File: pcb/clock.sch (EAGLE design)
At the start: 20 parts, among them IC1 74AHCT125, U1 ESP-01, U2 LD1117V33

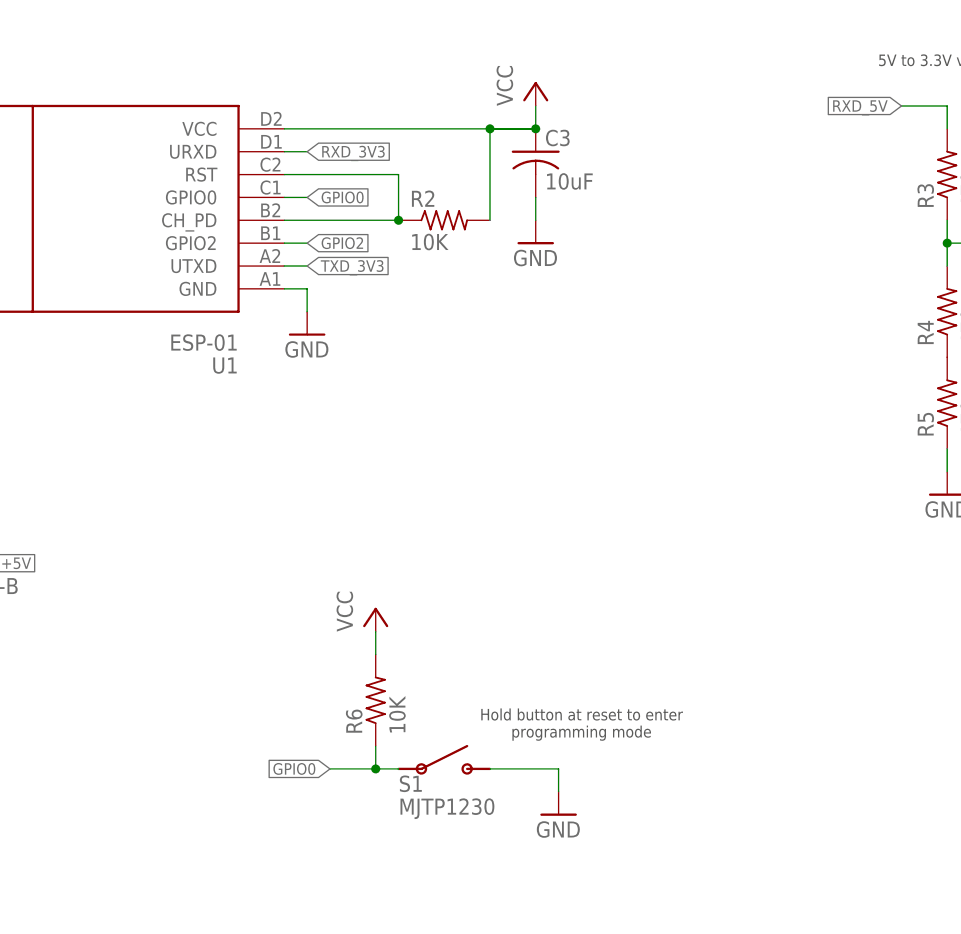
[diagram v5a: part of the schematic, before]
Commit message: Added DTR to RST pin
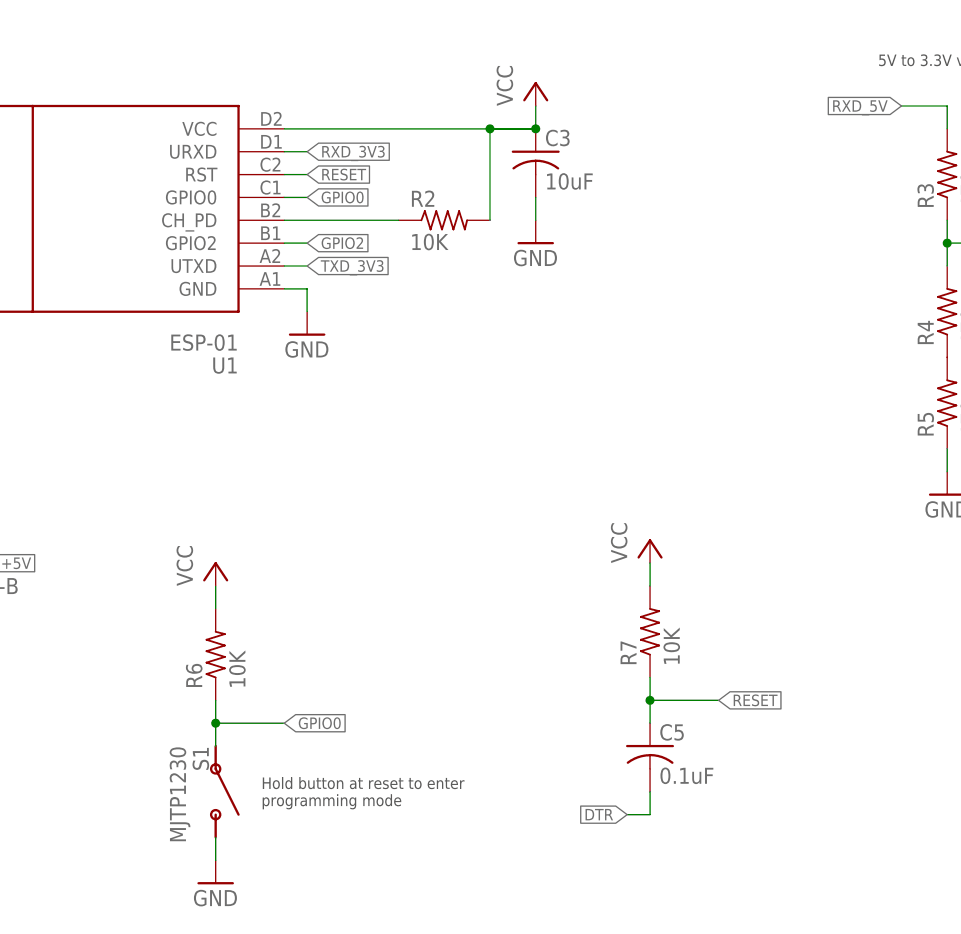
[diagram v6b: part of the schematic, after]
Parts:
- added C5: 0.1uF, rcl:C-US025-025X050
- added R7: 10K, rcl:R-US_0207/10
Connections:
- removed net N$2: R2.1, U1.CH_PD, U1.RST
- new net N$4: R2.1, U1.CH_PD
- new net RESET: C5.1, R7.1, U1.RST
- net DTR: now also C5.2
- net VCC: now also R7.2
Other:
- moved on the sheet: R6, S1
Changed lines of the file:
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@@
 <part name="GND11" library="supply1" deviceset="GND" device=""/>
 <part name="D1" library="diode" deviceset="1N581*" device="" technology="7-B"/>
+<part name="P+4" library="supply1" deviceset="VCC" device=""/>
+<part name="R7" library="rcl" deviceset="R-US_" device="0207/10" value="10K"/>
+<part name="C5" library="rcl" deviceset="C-US" device="025-025X050" value="0.1uF"/>
 </parts>
 <sheets>
 <sheet>
 <plain>
-<text x="114.3" y="40.64" size="1.27" layer="97" align="center">Hold button at reset to enter
+<text x="78.74" y="33.02" size="1.27" layer="97" align="center-left">Hold button at reset to enter
 programming mode</text>
 <text x="157.48" y="114.3" size="1.27" layer="97" align="center">5V to 3.3V voltage divider</text>
@@
 <instance part="IC1" gate="G$1" x="220.98" y="91.44"/>
 <instance part="GND8" gate="1" x="198.12" y="78.74"/>
-<instance part="S1" gate="G$1" x="99.06" y="35.56"/>
+<instance part="S1" gate="G$1" x="73.66" y="33.02" rot="R270"/>
 <instance part="GND9" gate="1" x="35.56" y="25.4"/>
-<instance part="GND10" gate="1" x="111.76" y="30.48"/>
-<instance part="P+3" gate="VCC" x="91.44" y="53.34"/>
-<instance part="R6" gate="G$1" x="91.44" y="43.18" rot="R90"/>
+<instance part="GND10" gate="1" x="73.66" y="22.86"/>
+<instance part="P+3" gate="VCC" x="73.66" y="58.42"/>
+<instance part="R6" gate="G$1" x="73.66" y="48.26" rot="R90"/>
 <instance part="H1" gate="G$1" x="177.8" y="162.56"/>
 <instance part="H2" gate="G$1" x="177.8" y="154.94"/>
 <instance part="GND11" gate="1" x="170.18" y="149.86"/>
 <instance part="D1" gate="G$1" x="43.18" y="58.42"/>
+<instance part="P+4" gate="VCC" x="121.92" y="60.96"/>
+<instance part="R7" gate="G$1" x="121.92" y="50.8" rot="R90"/>
+<instance part="C5" gate="G$1" x="121.92" y="38.1"/>
 </instances>
 <busses>
@@
 <pinref part="P+3" gate="VCC" pin="VCC"/>
 <pinref part="R6" gate="G$1" pin="2"/>
-<wire x1="91.44" y1="50.8" x2="91.44" y2="48.26" width="0.1524" layer="91"/>
+<wire x1="73.66" y1="55.88" x2="73.66" y2="53.34" width="0.1524" layer="91"/>
+</segment>
+<segment>
+<pinref part="P+4" gate="VCC" pin="VCC"/>
+<pinref part="R7" gate="G$1" pin="2"/>
+<wire x1="121.92" y1="58.42" x2="121.92" y2="55.88" width="0.1524" layer="91"/>
 </segment>
 </net>
@@
 <segment>
 <pinref part="S1" gate="G$1" pin="3"/>
-<wire x1="104.14" y1="35.56" x2="111.76" y2="35.56" width="0.1524" layer="91"/>
-<wire x1="111.76" y1="35.56" x2="111.76" y2="33.02" width="0.1524" layer="91"/>
+<wire x1="73.66" y1="27.94" x2="73.66" y2="25.4" width="0.1524" layer="91"/>
 <pinref part="GND10" gate="1" pin="GND"/>
 </segment>
@@
 <wire x1="43.18" y1="43.18" x2="35.56" y2="43.18" width="0.1524" layer="91"/>
 <label x="35.56" y="43.18" size="1.27" layer="95" rot="MR0" xref="yes"/>
+</segment>
+<segment>
+<pinref part="C5" gate="G$1" pin="2"/>
+<wire x1="121.92" y1="33.02" x2="121.92" y2="30.48" width="0.1524" layer="91"/>
+<wire x1="121.92" y1="30.48" x2="119.38" y2="30.48" width="0.1524" layer="91"/>
+<label x="119.38" y="30.48" size="1.27" layer="95" rot="R180" xref="yes"/>
 </segment>
 </net>
@@
 </segment>
 </net>
-<net name="N$2" class="0">
-<segment>
-<pinref part="U1" gate="G$1" pin="CH_PD"/>
-<pinref part="R2" gate="G$1" pin="1"/>
-<wire x1="81.28" y1="96.52" x2="93.98" y2="96.52" width="0.1524" layer="91"/>
-<pinref part="U1" gate="G$1" pin="RST"/>
-<wire x1="81.28" y1="101.6" x2="93.98" y2="101.6" width="0.1524" layer="91"/>
-<wire x1="93.98" y1="101.6" x2="93.98" y2="96.52" width="0.1524" layer="91"/>
-<junction x="93.98" y="96.52"/>
-</segment>
-</net>
 <net name="N$3" class="0">
 <segment>
@@
 <segment>
 <pinref part="S1" gate="G$1" pin="1"/>
-<wire x1="93.98" y1="35.56" x2="91.44" y2="35.56" width="0.1524" layer="91"/>
-<wire x1="91.44" y1="35.56" x2="86.36" y2="35.56" width="0.1524" layer="91"/>
-<wire x1="91.44" y1="35.56" x2="91.44" y2="38.1" width="0.1524" layer="91"/>
-<junction x="91.44" y="35.56"/>
+<wire x1="73.66" y1="38.1" x2="73.66" y2="40.64" width="0.1524" layer="91"/>
+<wire x1="73.66" y1="40.64" x2="81.28" y2="40.64" width="0.1524" layer="91"/>
+<wire x1="73.66" y1="40.64" x2="73.66" y2="43.18" width="0.1524" layer="91"/>
+<junction x="73.66" y="40.64"/>
 <pinref part="R6" gate="G$1" pin="1"/>
-<label x="86.36" y="35.56" size="1.27" layer="95" rot="R180" xref="yes"/>
+<label x="81.28" y="40.64" size="1.27" layer="95" xref="yes"/>
 </segment>
 </net>
@@
 </segment>
 </net>
+<net name="N$4" class="0">
+<segment>
+<pinref part="R2" gate="G$1" pin="1"/>
+<pinref part="U1" gate="G$1" pin="CH_PD"/>
+<wire x1="81.28" y1="96.52" x2="93.98" y2="96.52" width="0.1524" layer="91"/>
+</segment>
+</net>
+<net name="RESET" class="0">
+<segment>
+<pinref part="U1" gate="G$1" pin="RST"/>
+<wire x1="81.28" y1="101.6" x2="83.82" y2="101.6" width="0.1524" layer="91"/>
+<label x="83.82" y="101.6" size="1.27" layer="95" xref="yes"/>
+</segment>
+<segment>
+<wire x1="121.92" y1="40.64" x2="121.92" y2="43.18" width="0.1524" layer="91"/>
+<pinref part="R7" gate="G$1" pin="1"/>
+<pinref part="C5" gate="G$1" pin="1"/>
+<wire x1="121.92" y1="43.18" x2="121.92" y2="45.72" width="0.1524" layer="91"/>
+<wire x1="121.92" y1="43.18" x2="129.54" y2="43.18" width="0.1524" layer="91"/>
+<junction x="121.92" y="43.18"/>
+<label x="129.54" y="43.18" size="1.27" layer="95" xref="yes"/>
+</segment>
+</net>

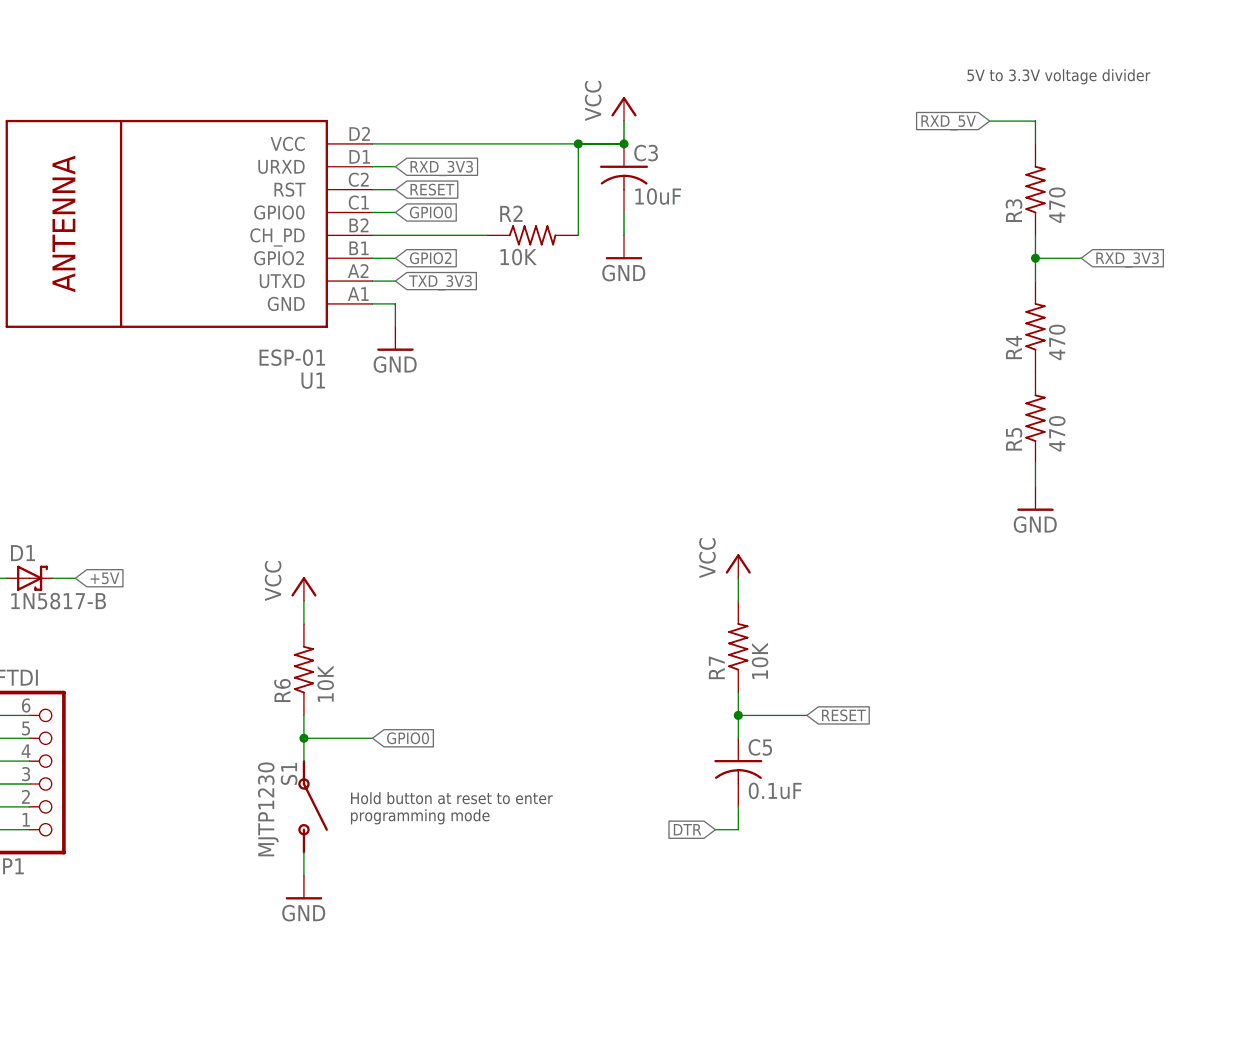
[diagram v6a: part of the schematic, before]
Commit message: Changed resistor size & voltage divider values
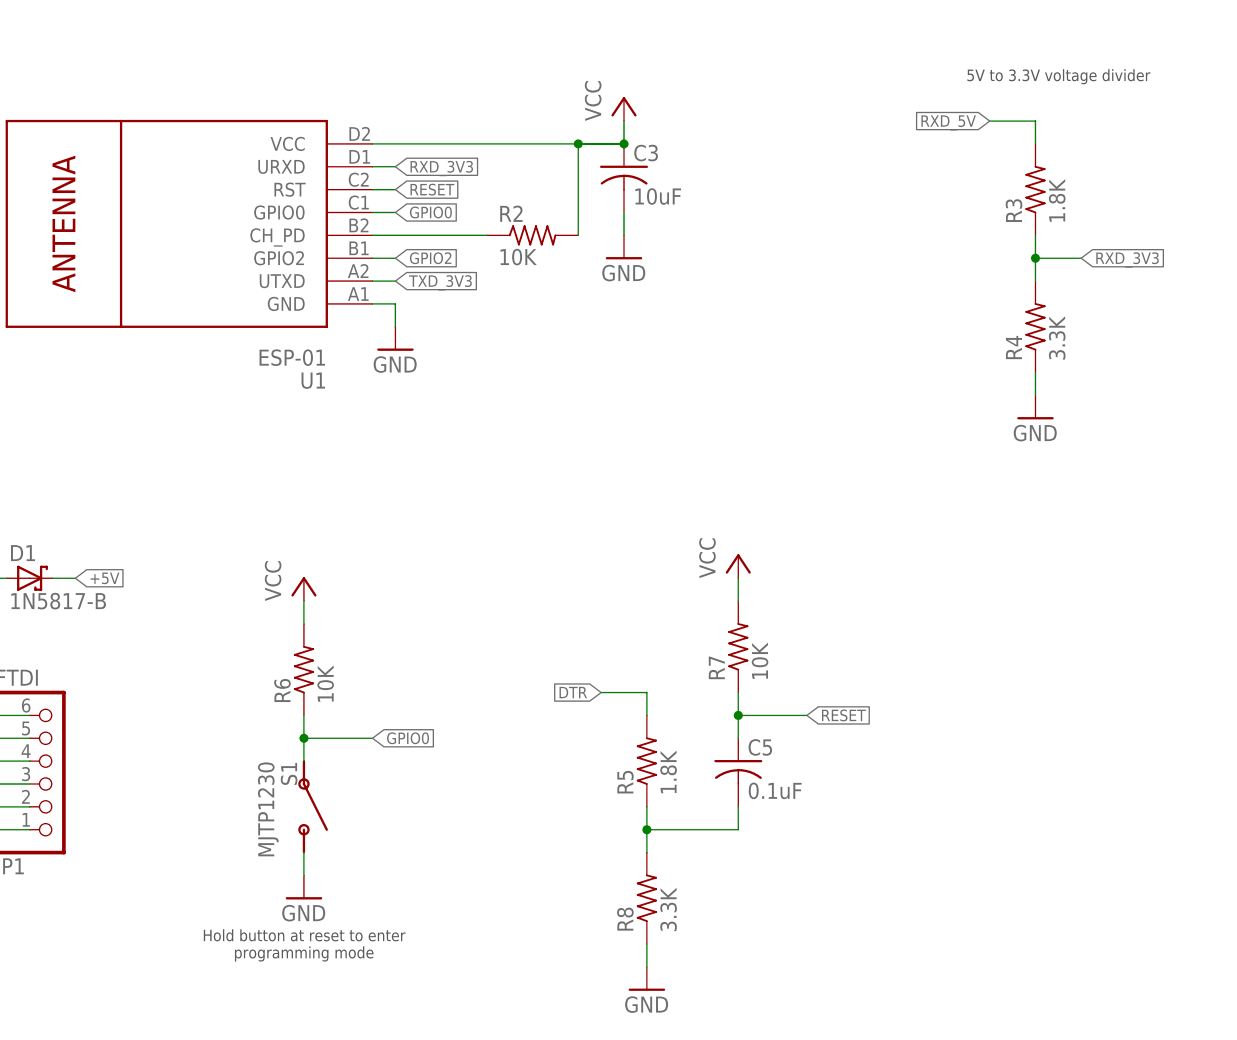
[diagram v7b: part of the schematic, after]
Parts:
- added R8: 3.3K, rcl:R-US_0204/5
- R1, R2, R6, R7: device rcl:R-US_0207/10 -> rcl:R-US_0204/5
- R3, R5: value 470 -> 1.8K; device rcl:R-US_0207/10 -> rcl:R-US_0204/5
- R4: value 470 -> 3.3K; device rcl:R-US_0207/10 -> rcl:R-US_0204/5
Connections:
- removed net N$3: R4.1, R5.2
- new net N$2: C5.2, R5.1, R8.2
- net DTR: now also R5.2; no longer C5.2
- net GND: now also R4.1, R8.1; no longer R5.1
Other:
- moved on the sheet: R5
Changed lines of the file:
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@@
 <part name="CN1" library="adafruit" deviceset="DCBARREL" device="PTH"/>
 <part name="GND4" library="supply1" deviceset="GND" device=""/>
-<part name="R1" library="rcl" deviceset="R-US_" device="0207/10" value="470"/>
+<part name="R1" library="rcl" deviceset="R-US_" device="0204/5" value="470"/>
 <part name="C4" library="rcl" deviceset="CPOL-US" device="E3.5-8" value="1000uF"/>
 <part name="GND5" library="supply1" deviceset="GND" device=""/>
 <part name="JP2" library="pinhead" deviceset="PINHD-1X2" device=""/>
 <part name="GND6" library="supply1" deviceset="GND" device=""/>
-<part name="R2" library="rcl" deviceset="R-US_" device="0207/10" value="10K"/>
-<part name="R3" library="rcl" deviceset="R-US_" device="0207/10" value="470"/>
-<part name="R4" library="rcl" deviceset="R-US_" device="0207/10" value="470"/>
-<part name="R5" library="rcl" deviceset="R-US_" device="0207/10" value="470"/>
+<part name="R2" library="rcl" deviceset="R-US_" device="0204/5" value="10K"/>
+<part name="R3" library="rcl" deviceset="R-US_" device="0204/5" value="1.8K"/>
+<part name="R4" library="rcl" deviceset="R-US_" device="0204/5" value="3.3K"/>
 <part name="GND7" library="supply1" deviceset="GND" device=""/>
 <part name="IC1" library="ic-package" deviceset="DIL14" device="" value="74AHCT125"/>
@@
 <part name="GND10" library="supply1" deviceset="GND" device=""/>
 <part name="P+3" library="supply1" deviceset="VCC" device=""/>
-<part name="R6" library="rcl" deviceset="R-US_" device="0207/10" value="10K"/>
+<part name="R6" library="rcl" deviceset="R-US_" device="0204/5" value="10K"/>
 <part name="H1" library="holes" deviceset="MOUNT-PAD-ROUND" device="2.8" value="MOUNT-PAD-ROUND2.8"/>
 <part name="H2" library="holes" deviceset="MOUNT-PAD-SQUARE" device="2.8"/>
@@
 <part name="D1" library="diode" deviceset="1N581*" device="" technology="7-B"/>
 <part name="P+4" library="supply1" deviceset="VCC" device=""/>
-<part name="R7" library="rcl" deviceset="R-US_" device="0207/10" value="10K"/>
+<part name="R7" library="rcl" deviceset="R-US_" device="0204/5" value="10K"/>
 <part name="C5" library="rcl" deviceset="C-US" device="025-025X050" value="0.1uF"/>
+<part name="R5" library="rcl" deviceset="R-US_" device="0204/5" value="1.8K"/>
+<part name="R8" library="rcl" deviceset="R-US_" device="0204/5" value="3.3K"/>
+<part name="GND12" library="supply1" deviceset="GND" device=""/>
 </parts>
 <sheets>
 <sheet>
 <plain>
-<text x="78.74" y="33.02" size="1.27" layer="97" align="center-left">Hold button at reset to enter
+<text x="73.66" y="17.78" size="1.27" layer="97" align="center">Hold button at reset to enter
 programming mode</text>
 <text x="157.48" y="114.3" size="1.27" layer="97" align="center">5V to 3.3V voltage divider</text>
@@
 <instance part="R3" gate="G$1" x="154.94" y="101.6" rot="R90"/>
 <instance part="R4" gate="G$1" x="154.94" y="86.36" rot="R90"/>
-<instance part="R5" gate="G$1" x="154.94" y="76.2" rot="R90"/>
-<instance part="GND7" gate="1" x="154.94" y="66.04"/>
+<instance part="GND7" gate="1" x="154.94" y="76.2"/>
 <instance part="IC1" gate="G$1" x="220.98" y="91.44"/>
 <instance part="GND8" gate="1" x="198.12" y="78.74"/>
@@
 <instance part="R7" gate="G$1" x="121.92" y="50.8" rot="R90"/>
 <instance part="C5" gate="G$1" x="121.92" y="38.1"/>
+<instance part="R5" gate="G$1" x="111.76" y="38.1" rot="R90"/>
+<instance part="R8" gate="G$1" x="111.76" y="22.86" rot="R90"/>
+<instance part="GND12" gate="1" x="111.76" y="12.7"/>
 </instances>
 <busses>
@@
 </segment>
 <segment>
-<pinref part="R5" gate="G$1" pin="1"/>
 <pinref part="GND7" gate="1" pin="GND"/>
-<wire x1="154.94" y1="71.12" x2="154.94" y2="68.58" width="0.1524" layer="91"/>
+<wire x1="154.94" y1="81.28" x2="154.94" y2="78.74" width="0.1524" layer="91"/>
+<pinref part="R4" gate="G$1" pin="1"/>
 </segment>
 <segment>
@@
 <junction x="175.26" y="154.94"/>
 </segment>
+<segment>
+<pinref part="R8" gate="G$1" pin="1"/>
+<pinref part="GND12" gate="1" pin="GND"/>
+<wire x1="111.76" y1="15.24" x2="111.76" y2="17.78" width="0.1524" layer="91"/>
+</segment>
 </net>
 <net name="TXD_5V" class="0">
@@
 </segment>
 <segment>
-<pinref part="C5" gate="G$1" pin="2"/>
-<wire x1="121.92" y1="33.02" x2="121.92" y2="30.48" width="0.1524" layer="91"/>
-<wire x1="121.92" y1="30.48" x2="119.38" y2="30.48" width="0.1524" layer="91"/>
-<label x="119.38" y="30.48" size="1.27" layer="95" rot="R180" xref="yes"/>
+<wire x1="111.76" y1="45.72" x2="106.68" y2="45.72" width="0.1524" layer="91"/>
+<label x="106.68" y="45.72" size="1.27" layer="95" rot="R180" xref="yes"/>
+<pinref part="R5" gate="G$1" pin="2"/>
+<wire x1="111.76" y1="45.72" x2="111.76" y2="43.18" width="0.1524" layer="91"/>
 </segment>
 </net>
@@
 </segment>
 </net>
-<net name="N$3" class="0">
-<segment>
-<pinref part="R4" gate="G$1" pin="1"/>
-<pinref part="R5" gate="G$1" pin="2"/>
-</segment>
-</net>
 <net name="GPIO2" class="0">
 <segment>
@@
 </segment>
 </net>
+<net name="N$2" class="0">
+<segment>
+<pinref part="R5" gate="G$1" pin="1"/>
+<pinref part="R8" gate="G$1" pin="2"/>
+<wire x1="111.76" y1="27.94" x2="111.76" y2="30.48" width="0.1524" layer="91"/>
+<pinref part="C5" gate="G$1" pin="2"/>
+<wire x1="111.76" y1="30.48" x2="111.76" y2="33.02" width="0.1524" layer="91"/>
+<wire x1="111.76" y1="30.48" x2="121.92" y2="30.48" width="0.1524" layer="91"/>
+<wire x1="121.92" y1="30.48" x2="121.92" y2="33.02" width="0.1524" layer="91"/>
+<junction x="111.76" y="30.48"/>
+</segment>
+</net>
